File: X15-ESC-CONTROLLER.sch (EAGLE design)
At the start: 15 parts, among them J1 3V3 -SWCLK-GND-SWDIO- NRST

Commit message: Design Review Push
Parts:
- added C7, C8: 20pF, SparkFun-Capacitors:20PF-0402T-50V-5%
- added IC1, IC2: OP-AMP, SparkFun-IC-Amplifiers:OPAMP-DUALU
- added JP1: JUMPER-SMT_2_NO_NO-SILK, SparkFun-Jumpers:JUMPER-SMT_2_NO_NO-SILK
- added R4: 1k, SparkFun-Resistors:1KOHM-0603-1/10W-1%
- added R5: 3.3k, SparkFun-Resistors:1KOHM-0603-1/10W-1%
- added U$3, U$4: JST_8_PIN, X15-Parts-Library:JST_8_PIN
- added U$5: BAKCPLANE_CONNECTOR, X15-Parts-Library:BAKCPLANE_CONNECTOR
- added Y1: ECS-80-S-4X, ECS-80-S-4X:ECS-80-S-4X
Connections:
- new net ADC_1: U$3.ADC
- new net ADC_2: U$1.PB7, U$4.ADC
- new net ESC_ID: U$5.12
- new net N$6: C7.1, Y1.2
- new net N$7: C8.1, Y1.1
- net +3V3: now also C4.1, IC1G3.P$V+, R4.2, U$1.VDDA, U$5.1, U$5.2, U$5.3, U$5.4
- net CAN_H: now also U$5.5
- net CAN_L: now also U$5.7
- net GND: now also C7.2, C8.2, IC1G3.P$V-, R5.1, U$3.LIPO_GND, U$4.LIPO_GND, U$5.10
- net N$3: now also IC1G2.-IN, R4.1, R5.2; no longer C4.1, U$1.VDDA
- net NRST: now also U$5.6
- net SWCLK: now also U$5.11
- net SWDIO: now also U$5.9
- net TIM1_CH1: now also U$3.MTR_1
- net TIM1_CH2: now also U$3.MTR_2
- net TIM1_CH3: now also U$3.MTR_3
- net TIM1_CH4: now also U$3.MTR_4
- net TIM1_CH5: now also U$4.MTR_1
- net TIM1_CH6: now also U$4.MTR_2
- net TIM1_CH7: now also U$4.MTR_3
- net TIM1_CH8: now also U$4.MTR_4
- net TLM: now also IC1G2.OUT, JP1.2
- net TLM_ESC: now also IC1G2.+IN, JP1.1, U$3.TLM, U$4.TLM

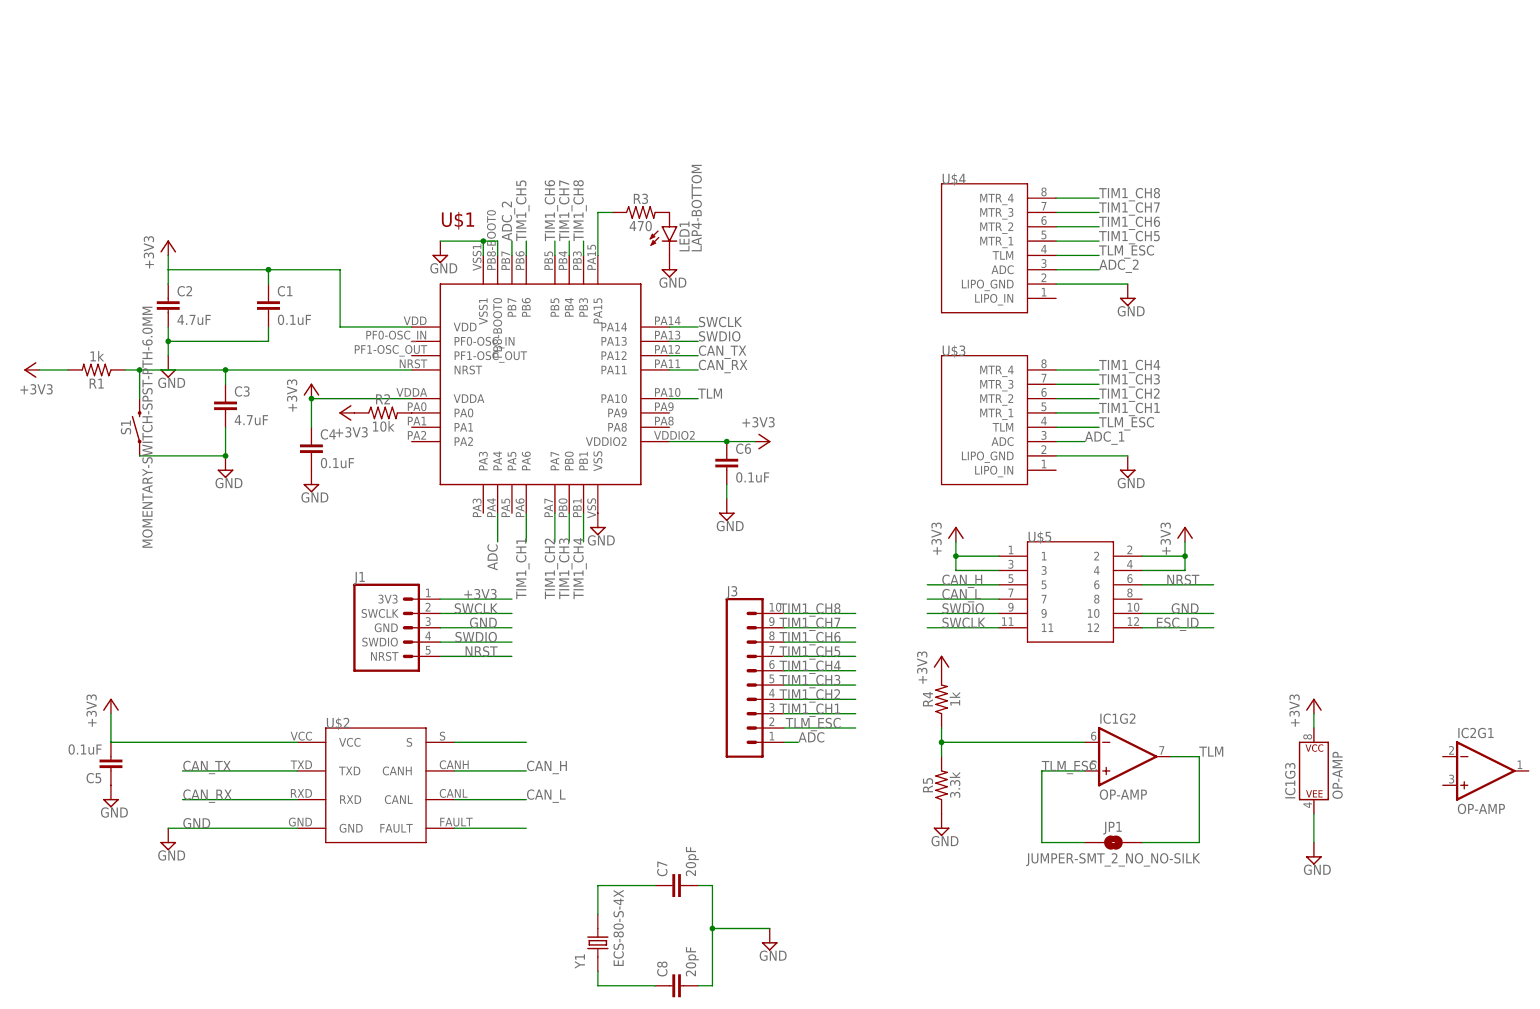
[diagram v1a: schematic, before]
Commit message: 3rd Esc added
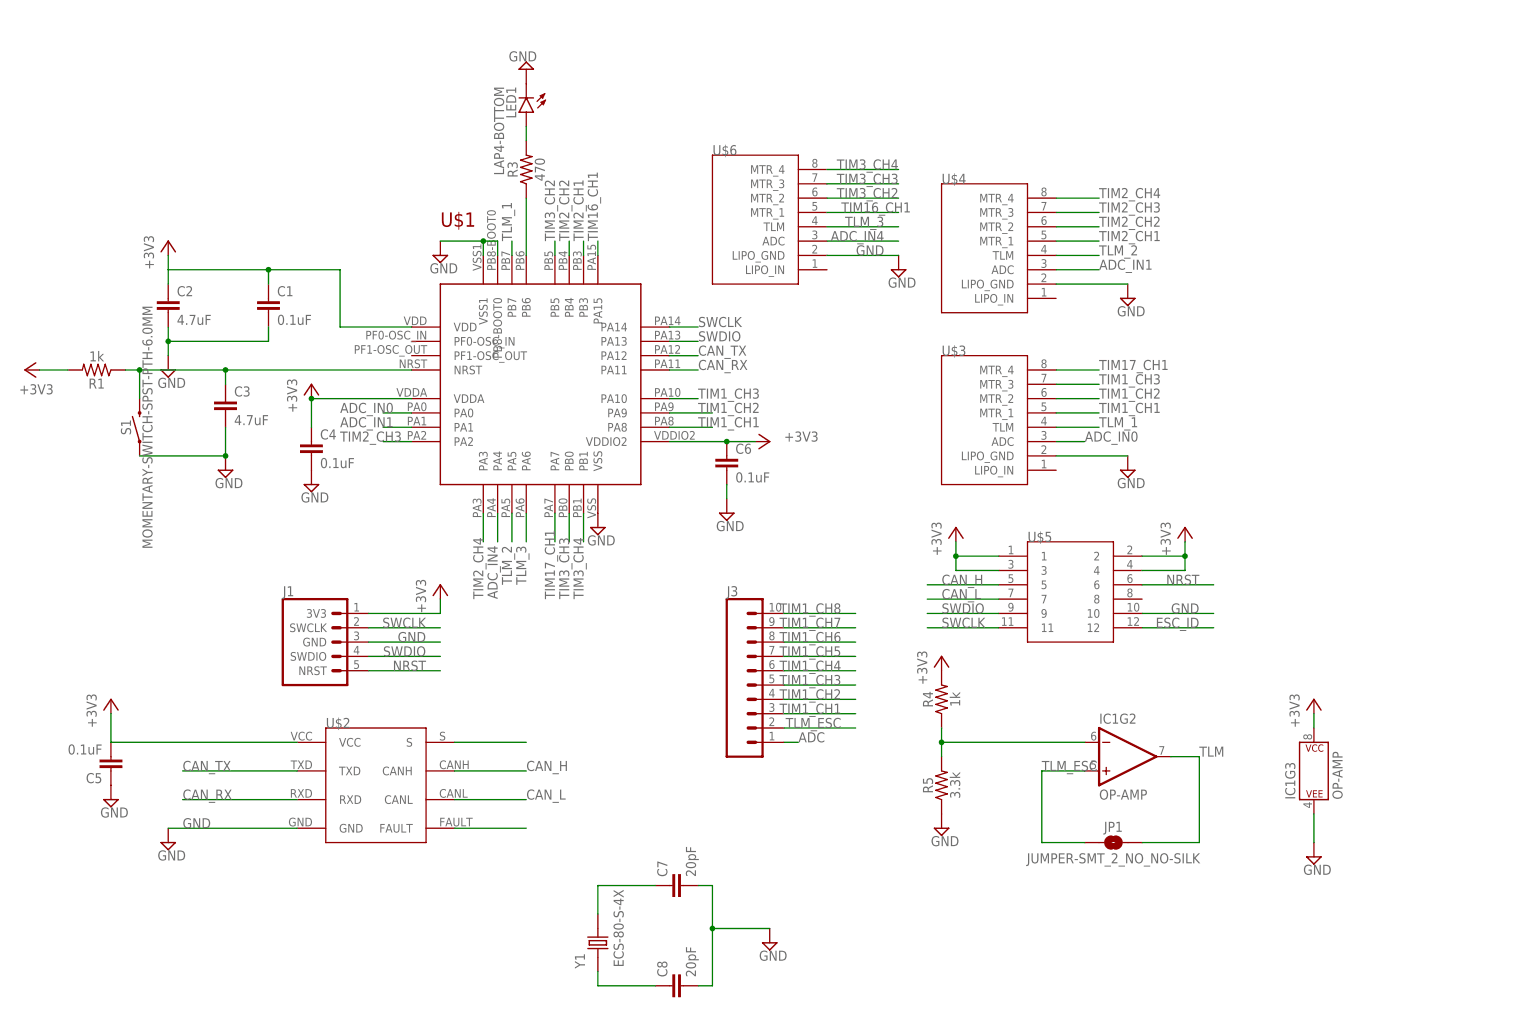
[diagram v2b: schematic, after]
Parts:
- removed IC2: OP-AMP, SparkFun-IC-Amplifiers:OPAMP-DUALU
- removed R2: 10k, SparkFun-Resistors:10KOHM-0603-1/10W-1%
- added U$6: JST_8_PIN, X15-Parts-Library:JST_8_PIN
- Y1: device ECS-80-S-4X:ECS-80-S-4X -> X15-Parts-Library:ECS-80-S-4X
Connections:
- removed net ADC_1: U$3.ADC
- removed net ADC_2: U$1.PB7, U$4.ADC
- removed net N$8 (its old number): R3.1, U$1.PA15
- new net ADC_IN0: U$1.PA0, U$3.ADC
- new net ADC_IN1: U$1.PA1, U$4.ADC
- new net ADC_IN4: U$1.PA4, U$6.ADC
- new net TIM16_CH1: U$1.PA15, U$6.MTR_1
- new net TIM17_CH1: U$1.PA7, U$3.MTR_4
- new net TIM2_CH1: U$1.PB3, U$4.MTR_1
- new net TIM2_CH2: U$1.PB4, U$4.MTR_2
- new net TIM2_CH3: U$1.PA2, U$4.MTR_3
- new net TIM2_CH4: U$1.PA3, U$4.MTR_4
- new net TIM3_CH2: U$1.PB5, U$6.MTR_2
- new net TIM3_CH3: U$1.PB0, U$6.MTR_3
- new net TIM3_CH4: U$1.PB1, U$6.MTR_4
- new net TLM_1: U$1.PB7, U$3.TLM
- new net TLM_2: U$1.PA5, U$4.TLM
- new net TLM_3: U$1.PA6, U$6.TLM
- net +3V3: no longer R2.1
- net ADC: no longer U$1.PA4
- net GND: now also U$6.LIPO_GND
- net N$4: now also R3.1, U$1.PB6; no longer R2.2, U$1.PA0
- net TIM1_CH1: now also U$1.PA8; no longer U$1.PA6
- net TIM1_CH2: now also U$1.PA9; no longer U$1.PA7
- net TIM1_CH3: now also U$1.PA10; no longer U$1.PB0
- net TIM1_CH4: no longer U$1.PB1, U$3.MTR_4
- net TIM1_CH5: no longer U$1.PB6, U$4.MTR_1
- net TIM1_CH6: no longer U$1.PB5, U$4.MTR_2
- net TIM1_CH7: no longer U$1.PB4, U$4.MTR_3
- net TIM1_CH8: no longer U$1.PB3, U$4.MTR_4
- net TLM: no longer U$1.PA10
- net TLM_ESC: no longer U$3.TLM, U$4.TLM
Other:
- moved on the sheet: J1, LED1, R3

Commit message: Board Edits
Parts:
- removed LED1: LAP4-BOTTOM, led:LAP4-BOTTOM
- removed S1: MOMENTARY-SWITCH-SPST-PTH-6.0MM, SparkFun-Switches:MOMENTARY-SWITCH-SPST-PTH-6.0MM
- added D1: COLOR, LED, 0805:LED-0805
- added J2, J4: (no value), SparkFun-Connectors:CONN_06NO_SILK_NO_POP
- added U$7: (no value), OTHER, Push button - FSM2JMTR:DISCRETECOMPONENTS_SWITCH
- J1: device X15-Parts-Library:SWD_CONN -> X15-ESC-Controller-Parts-Library:SWD_CONN
- J3: device SparkFun-Connectors:CONN_10" -> SparkFun-Connectors:CONN_06NO_SILK_NO_POP
- U$1: device X15-Parts-Library:STM32F042K6T6 -> X15-ESC-Controller-Parts-Library:STM32F042K6T6
- U$2: device X15-Parts-Library:TCAN337D -> X15-ESC-Controller-Parts-Library:TCAN337D
- U$3, U$4, U$6: device X15-Parts-Library:JST_8_PIN -> X15-ESC-Controller-Parts-Library:JST_8_PIN
- U$5: device X15-Parts-Library:BAKCPLANE_CONNECTOR -> X15-ESC-Controller-Parts-Library:BAKCPLANE_CONNECTOR
- Y1: device X15-Parts-Library:ECS-80-S-4X -> X15-ESC-Controller-Parts-Library:ECS-80-S-4X
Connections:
- removed net ADC: J3.1
- removed net N$1: C1.1, C2.1, U$1.VDD
- removed net N$5: C5.2, U$2.VCC
- removed net TIM1_CH4: J3.6
- removed net TIM1_CH5: J3.7
- removed net TIM1_CH6: J3.8
- removed net TIM1_CH7: J3.9
- removed net TIM1_CH8: J3.10
- net +3V3: now also C1.1, C2.1, C5.2, U$1.VDD, U$2.VCC
- net ADC_IN0: now also J4.1
- net ADC_IN1: now also J3.1
- net ADC_IN4: now also J2.1
- net GND: now also D1.C, U$7.P$1; no longer LED1.C, S1.1
- net N$2: now also U$7.P$2; no longer S1.2
- net N$8: now also D1.A; no longer LED1.A
- net TIM16_CH1: now also J2.3
- net TIM17_CH1: now also J4.6
- net TIM1_CH1: now also J4.3; no longer J3.3
- net TIM1_CH2: no longer J3.4
- net TIM1_CH3: now also J4.5; no longer J3.5
- net TIM2_CH1: now also J3.3
- net TIM2_CH2: now also J3.4, J4.4
- net TIM2_CH3: now also J3.5
- net TIM2_CH4: now also J3.6
- net TIM3_CH2: now also J2.4
- net TIM3_CH3: now also J2.5
- net TIM3_CH4: now also J2.6
- net TLM_1: now also J4.2
- net TLM_2: now also J3.2
- net TLM_3: now also J2.2
- net TLM_ESC: no longer J3.2
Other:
- moved on the sheet: U$5

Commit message: Final Board Edits
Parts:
- removed J4: (no value), SparkFun-Connectors:CONN_06NO_SILK_NO_POP
- added D2: COLOR, LED, 0805:LED-0805
- added R2: 150, SparkFun-Resistors:1KOHM-0603-1/10W-1%
- U$3, U$4, U$6: device X15-ESC-Controller-Parts-Library:JST_8_PIN -> X15-Parts-Library:JST_8_PIN
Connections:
- removed net TLM_1: J4.2, U$1.PB7, U$3.TLM
- removed net TLM_2: J3.2, U$1.PA5, U$4.TLM
- removed net TLM_3: J2.2, U$1.PA6, U$6.TLM
- new net N$1: D2.A, R2.2
- net +3V3: now also R2.1
- net ADC_IN0: no longer J4.1
- net GND: now also D2.C
- net TIM17_CH1: no longer J4.6
- net TIM1_CH1: no longer J4.3
- net TIM1_CH3: no longer J4.5
- net TIM2_CH2: no longer J4.4
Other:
- moved on the sheet: J1, J2, U$6

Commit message: Hopeful Final Push
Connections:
- net TLM renamed N$10
- net TLM_ESC renamed N$5
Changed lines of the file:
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@@
-</segment>
-</net>
-<net name="TLM" class="0">
-<segment>
-<wire x1="129.54" y1="12.7" x2="134.62" y2="12.7" width="0.1524" layer="91"/>
-<wire x1="134.62" y1="12.7" x2="134.62" y2="-2.54" width="0.1524" layer="91"/>
-<pinref part="JP1" gate="G$1" pin="2"/>
-<wire x1="134.62" y1="-2.54" x2="124.46" y2="-2.54" width="0.1524" layer="91"/>
-<pinref part="IC1" gate="G2" pin="OUT"/>
-</segment>
-</net>
-<net name="TLM_ESC" class="0">
-<segment>
-<pinref part="JP1" gate="G$1" pin="1"/>
-<wire x1="114.3" y1="-2.54" x2="106.68" y2="-2.54" width="0.1524" layer="91"/>
-<wire x1="106.68" y1="-2.54" x2="106.68" y2="10.16" width="0.1524" layer="91"/>
-<wire x1="106.68" y1="10.16" x2="114.3" y2="10.16" width="0.1524" layer="91"/>
-<pinref part="IC1" gate="G2" pin="+IN"/>
 </segment>
 </net>
@@
 </segment>
 </net>
+<net name="N$5" class="0">
+<segment>
+<pinref part="IC1" gate="G2" pin="+IN"/>
+<wire x1="114.3" y1="10.16" x2="109.22" y2="10.16" width="0.1524" layer="91"/>
+<wire x1="109.22" y1="10.16" x2="109.22" y2="-2.54" width="0.1524" layer="91"/>
+<pinref part="JP1" gate="G$1" pin="1"/>
+<wire x1="109.22" y1="-2.54" x2="114.3" y2="-2.54" width="0.1524" layer="91"/>
+</segment>
+</net>
+<net name="N$10" class="0">
+<segment>
+<pinref part="JP1" gate="G$1" pin="2"/>
+<wire x1="124.46" y1="-2.54" x2="134.62" y2="-2.54" width="0.1524" layer="91"/>
+<wire x1="134.62" y1="-2.54" x2="134.62" y2="12.7" width="0.1524" layer="91"/>
+<pinref part="IC1" gate="G2" pin="OUT"/>
+<wire x1="134.62" y1="12.7" x2="129.54" y2="12.7" width="0.1524" layer="91"/>
+</segment>
+</net>
